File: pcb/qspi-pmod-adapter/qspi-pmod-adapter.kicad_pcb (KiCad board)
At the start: 2 copper layers, 33 x 16.5 mm, 10 parts, among them J1 PMOD plug, J2 PMOD socket, J3 Tiny QSPI socket, U1 W25Q128JVS

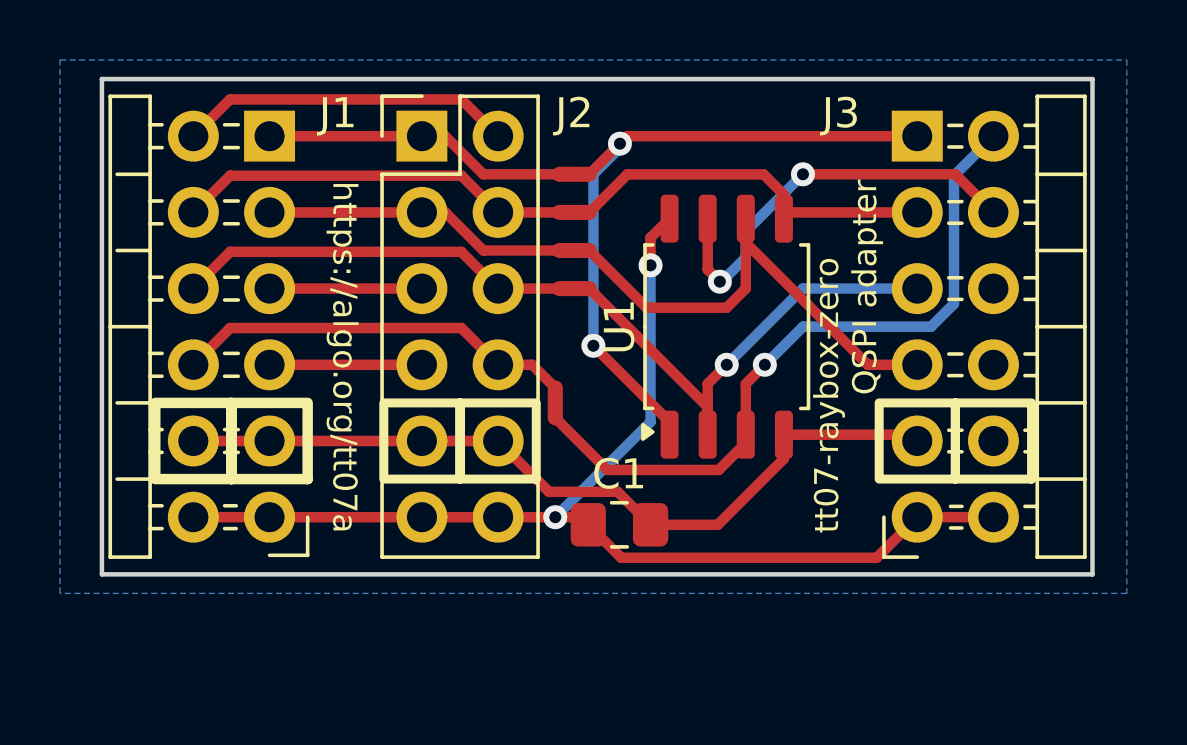
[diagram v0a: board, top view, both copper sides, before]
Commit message: tt07b (r1) PCB revision: QSPI adapter dual-plug [no ci]
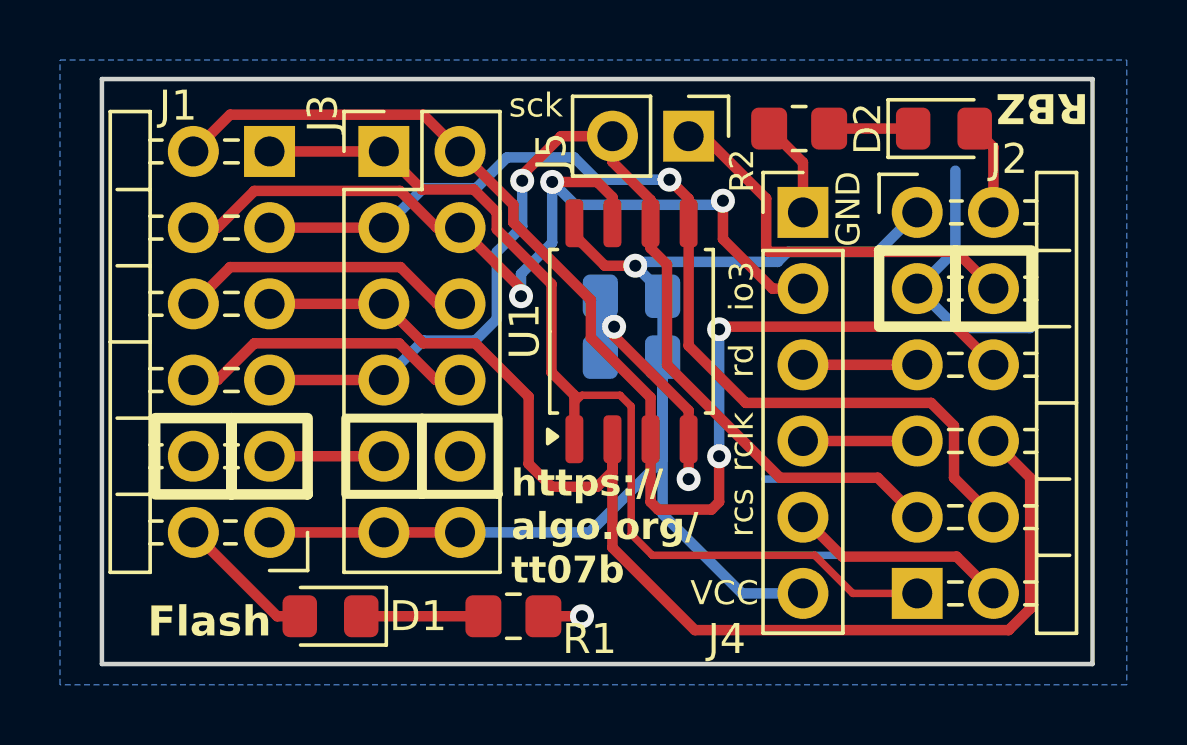
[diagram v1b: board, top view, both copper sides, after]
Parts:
- removed NT1, NT2, NT3, NT4, NT5: NetTie_2, NetTie:NetTie-2_SMD_Pad0.5mm
- added C2: 100nF, Capacitor_SMD:C_0805_2012Metric_Pad1.18x1.45mm_HandSolder, B.Cu at (116.2, 77.2)
- added D1: Red, LED_SMD:LED_0805_2012Metric_Pad1.15x1.40mm_HandSolder, F.Cu at (106.2, 85.9)
- added D2: Green, LED_SMD:LED_0805_2012Metric_Pad1.15x1.40mm_HandSolder, F.Cu at (126.6, 69.6)
- added J4: Conn_01x06, Connector_PinHeader_2.54mm:PinHeader_1x06_P2.54mm_Vertical, F.Cu at (121.9, 72.4)
- added J5: Conn_01x02_Pin, Connector_PinHeader_2.54mm:PinHeader_1x02_P2.54mm_Vertical, F.Cu at (118.1, 69.8)
- added R1: 330, Resistor_SMD:R_0805_2012Metric_Pad1.20x1.40mm_HandSolder, F.Cu at (112.3, 85.9)
- added R2: 330, Resistor_SMD:R_0805_2012Metric_Pad1.20x1.40mm_HandSolder, F.Cu at (121.8, 69.6)
- C1: moved to B.Cu
- J1: value PMOD plug -> PMOD plug: FLASHER
- J2: value PMOD socket -> PMOD plug: RBZ; footprint Anton Kicad Footprints Lib:PinSocket_2x06_P2.54mm_PMODPeriph2B_Vertical -> Anton Kicad Footprints Lib:PinHeader_2x06_P2.54mm_PMODPeriph2B_Clip
- J3: footprint Anton Kicad Footprints Lib:PinSocket_2x06_P2.54mm_PMODPeriph2B_Clip -> Anton Kicad Footprints Lib:PinSocket_2x06_P2.54mm_PMODPeriph2B_Vertical
- moved J2 19.4 mm to (125.7, 72.4), turned to 0 degrees
- moved J3 17.8 mm to (108.0, 83.1)
- moved C1 7.63 mm to (116.2, 75.2), turned to 180 degrees
- moved U1 3.18 mm to (116.2, 76.4)
- moved J1 0.51 mm to (104.1, 83.1)
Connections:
- J1 pad 1: /uio0 -> /~{CS0}
- J1 pad 10: /uio7 -> /~{CS2}
- J1 pad 12: VCC -> Net-(D1-A)
- J1 pad 2: /uio1 -> /io0
- J1 pad 3: /uio2 -> /io1
- J1 pad 4: /uio3 -> /SCK
- J1 pad 7: /uio4 -> /io2
- J1 pad 8: /uio5 -> /io3
- J1 pad 9: /uio6 -> /~{CS1}
- J2 pad 1: /uio0 -> /~{CS0}
- J2 pad 10: /uio7 -> /io2
- J2 pad 11: GND -> Net-(J2-Pin_11)
- J2 pad 12: VCC -> Net-(D2-A)
- J2 pad 2: /uio1 -> /SCK
- J2 pad 3: /uio2 -> /rsck
- J2 pad 4: /uio3 -> /rmosi
- J2 pad 7: /uio4 -> /rcsb
- J2 pad 8: /uio5 -> /io0
- J2 pad 9: /uio6 -> /io1
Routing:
- net /io1: track 16.5 -> 41.6 mm, vias 1 -> 0
- net /io0: track 12.6 -> 33.9 mm, vias 0 -> 1
- net /SCK: track 16.0 -> 35.9 mm, vias 0 -> 1
- net /io2: track 23.6 -> 42.2 mm, vias 1 -> 2
- net /io3: track 13.9 -> 31.1 mm, vias 2 -> 3
- net /uio7: track 13.4 -> 0.00 mm
- net Net-(J2-Pin_11): track 0.00 -> 13.3 mm
- net /uio6: track 13.2 -> 0.00 mm
- net /uio5: track 13.2 -> 0.00 mm
- net /~{CS0}: track 22.6 -> 35.0 mm, vias 2 -> 0
- net /uio4: track 11.2 -> 0.00 mm
- net /uio0: track 10.2 -> 0.00 mm
- net /uio1: track 10.2 -> 0.00 mm
- net /~{CS1}: track 0.00 -> 9.90 mm
- net /~{CS2}: track 0.00 -> 9.90 mm
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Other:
- board size 33 x 16.5 mm -> 33 x 19.5 mm
- board text added: "Flash"
- board text added: "GND"
- board text added: "JLCJLCJLCJLC"
- board text added: "Plug in QSPI PMOD"
- board text added: "Plug in for using raybox-zero"
- board text added: "Plug in for writing to flash"
- board text added: "RBZ"
- board text added: "VCC"
- board text added: "https:// algo.org/ tt07b"
- board text added: "io3"
- board text added: "rclk"
- board text added: "rcs"
- board text added: "rd"
- board text added: "sck"
- board text added: "tt07-raybox-zero QSPI adapter r1"
- board text removed: "PMOD pass-thru socket"
- board text removed: "Plug Tiny QSPI PMOD in"
- board text removed: "Plug into demo board"
- board text removed: "QSPI adapter"
- board text removed: "https://algo.org/tt07a"
- board text removed: "tt07-raybox-zero"
